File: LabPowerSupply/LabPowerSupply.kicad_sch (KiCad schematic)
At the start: 2 parts

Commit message: Began mcu placement
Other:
- sheet Primary Controller ports: added ADC 4; removed ADC 0
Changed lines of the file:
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@@
       (effects (font (size 1.27 1.27)) (justify right))
     )
-    (pin "ADC 0" input (at 182.88 71.12 180)
-      (effects (font (size 1.27 1.27)) (justify left))
-    )
-    (pin "ADC 2" input (at 182.88 76.2 180)
-      (effects (font (size 1.27 1.27)) (justify left))
-    )
-    (pin "ADC 1" input (at 182.88 73.66 180)
-      (effects (font (size 1.27 1.27)) (justify left))
-    )
-    (pin "ADC 3" input (at 182.88 78.74 180)
+    (pin "ADC 1" input (at 182.88 71.12 180)
+      (effects (font (size 1.27 1.27)) (justify left))
+    )
+    (pin "ADC 3" input (at 182.88 76.2 180)
+      (effects (font (size 1.27 1.27)) (justify left))
+    )
+    (pin "ADC 2" input (at 182.88 73.66 180)
+      (effects (font (size 1.27 1.27)) (justify left))
+    )
+    (pin "ADC 4" input (at 182.88 78.74 180)
       (effects (font (size 1.27 1.27)) (justify left))
     )
@@
       (reference "C10_Power1") (unit 1) (value "100n") (footprint "Capacitor_SMD:C_0603_1608Metric")
     )
+    (path "/0c3af00c-caea-46d1-9953-712c4efb6180/877b38b4-9fca-4c7e-a1c5-d7e6e745bcaf/f3b7bb4f-3c1d-4dfa-8749-a3a16444aa2b"
+      (reference "C_CUR1") (unit 1) (value "100n") (footprint "Capacitor_SMD:C_0603_1608Metric")
+    )
+    (path "/e157f35d-29d6-4a10-895b-6361f5380fc1/877b38b4-9fca-4c7e-a1c5-d7e6e745bcaf/f3b7bb4f-3c1d-4dfa-8749-a3a16444aa2b"
+      (reference "C_CUR2") (unit 1) (value "100n") (footprint "Capacitor_SMD:C_0603_1608Metric")
+    )
+    (path "/0c3af00c-caea-46d1-9953-712c4efb6180/1f8c5f30-7c48-4f7f-ae89-842563537cb2/8593098b-f15d-439b-8094-0023f0ebc382"
+      (reference "C_INV1") (unit 1) (value "100n") (footprint "Capacitor_SMD:C_0603_1608Metric")
+    )
+    (path "/e157f35d-29d6-4a10-895b-6361f5380fc1/1f8c5f30-7c48-4f7f-ae89-842563537cb2/8593098b-f15d-439b-8094-0023f0ebc382"
+      (reference "C_INV2") (unit 1) (value "100n") (footprint "Capacitor_SMD:C_0603_1608Metric")
+    )
+    (path "/3d294f79-f2d7-4288-8001-342bbe758cab/6678ab0e-55b4-4de2-ab64-1e272bb328a1"
+      (reference "C_OPT1") (unit 1) (value "100n") (footprint "Capacitor_SMD:C_0603_1608Metric")
+    )
+    (path "/3d294f79-f2d7-4288-8001-342bbe758cab/b5ccd18e-1d8f-4940-b38a-e2dbf67af339"
+      (reference "C_OPT2") (unit 1) (value "100n") (footprint "Capacitor_SMD:C_0603_1608Metric")
+    )
     (path "/0c3af00c-caea-46d1-9953-712c4efb6180/877b38b4-9fca-4c7e-a1c5-d7e6e745bcaf/ad5d9838-b611-434b-a2e7-188d7ef8b357"

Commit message: Started ch2 MCU routing
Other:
- sheet Primary Controller ports: added DAC 2; removed DAC 0
- sheet Secondary Controller ports: added ADC 4, DAC 2; removed ADC 0, DAC 0
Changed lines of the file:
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@@
       (effects (font (size 1.27 1.27)) (justify left top) hide)
     )
-    (pin "DAC 1" output (at 203.2 71.12 0)
+    (pin "DAC 2" output (at 203.2 71.12 0)
       (effects (font (size 1.27 1.27)) (justify right))
     )
@@
       (effects (font (size 1.27 1.27)) (justify right))
     )
-    (pin "DAC 0" output (at 203.2 68.58 0)
+    (pin "DAC 1" output (at 203.2 68.58 0)
       (effects (font (size 1.27 1.27)) (justify right))
     )
@@
       (effects (font (size 1.27 1.27)) (justify right))
     )
-    (pin "ADC 3" input (at 182.88 109.22 180)
-      (effects (font (size 1.27 1.27)) (justify left))
-    )
-    (pin "ADC 0" input (at 182.88 101.6 180)
-      (effects (font (size 1.27 1.27)) (justify left))
-    )
-    (pin "ADC 1" input (at 182.88 104.14 180)
-      (effects (font (size 1.27 1.27)) (justify left))
-    )
-    (pin "ADC 2" input (at 182.88 106.68 180)
-      (effects (font (size 1.27 1.27)) (justify left))
-    )
-    (pin "DAC 1" output (at 203.2 101.6 0)
-      (effects (font (size 1.27 1.27)) (justify right))
-    )
-    (pin "DAC 0" output (at 203.2 99.06 0)
+    (pin "ADC 4" input (at 182.88 109.22 180)
+      (effects (font (size 1.27 1.27)) (justify left))
+    )
+    (pin "ADC 1" input (at 182.88 101.6 180)
+      (effects (font (size 1.27 1.27)) (justify left))
+    )
+    (pin "ADC 2" input (at 182.88 104.14 180)
+      (effects (font (size 1.27 1.27)) (justify left))
+    )
+    (pin "ADC 3" input (at 182.88 106.68 180)
+      (effects (font (size 1.27 1.27)) (justify left))
+    )
+    (pin "DAC 2" output (at 203.2 101.6 0)
+      (effects (font (size 1.27 1.27)) (justify right))
+    )
+    (pin "DAC 1" output (at 203.2 99.06 0)
       (effects (font (size 1.27 1.27)) (justify right))
     )
@@
       (reference "J_STLink1") (unit 1) (value "Conn_01x06_Male") (footprint "Connector_PinHeader_2.54mm:PinHeader_1x06_P2.54mm_Vertical")
     )
-    (path "/67b0d6de-a54b-4bd2-af78-b383bfe8d0e6/24e68b72-506f-44a1-bcfd-b573b2c4c581"
-      (reference "J_STLink2") (unit 1) (value "Conn_01x05_Male") (footprint "Connector_PinHeader_2.54mm:PinHeader_1x05_P2.54mm_Vertical")
+    (path "/67b0d6de-a54b-4bd2-af78-b383bfe8d0e6/08b4800b-af53-4276-a503-6ae9edd2289e"
+      (reference "J_STLink2") (unit 1) (value "Conn_01x06_Male") (footprint "Connector_PinHeader_2.54mm:PinHeader_1x06_P2.54mm_Vertical")
     )
     (path "/08fd45d5-b4ab-46e8-a348-5c4ac8e52155/d2de2ac8-3643-4f24-819b-2a4facabaee8"

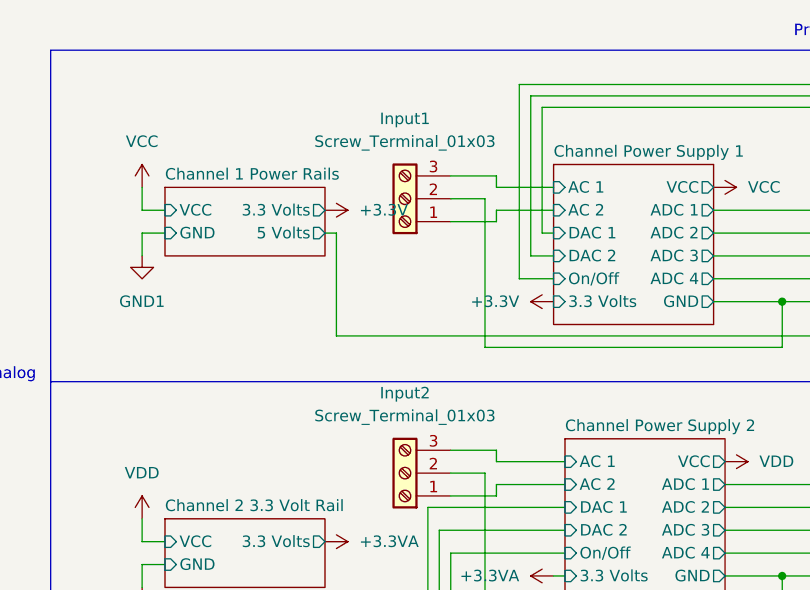
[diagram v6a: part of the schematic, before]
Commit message: Updated Part List
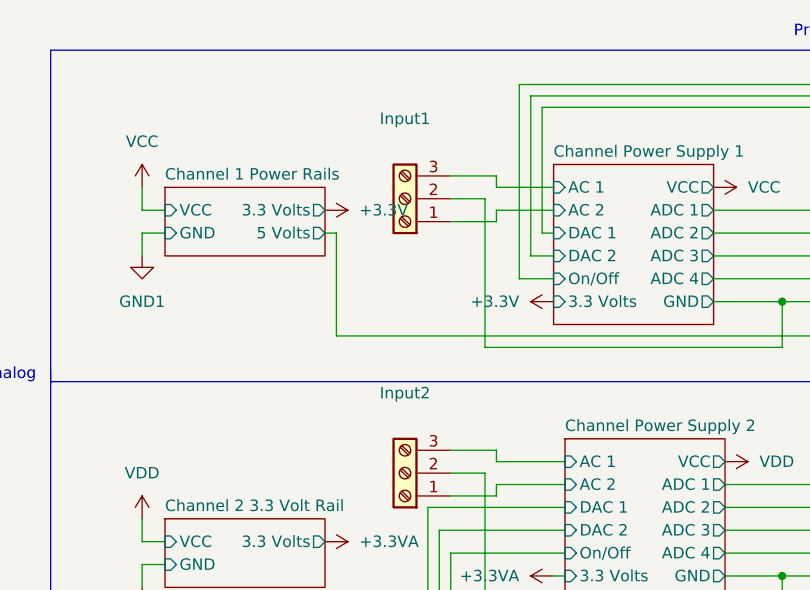
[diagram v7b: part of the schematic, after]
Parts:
- Input1, Input2: value Screw_Terminal_01x03 -> (none); footprint TerminalBlock:TerminalBlock_Altech_AK300-3_P5.00mm -> (none)
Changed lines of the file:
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@@
     (in_bom yes) (on_board yes) (fields_autoplaced)
     (property "Reference" "Input2" (id 0) (at 110.49 91.44 0))
-    (property "Value" "Screw_Terminal_01x03" (id 1) (at 110.49 93.98 0))
-    (property "Footprint" "TerminalBlock:TerminalBlock_Altech_AK300-3_P5.00mm" (id 2) (at 110.49 100.33 0)
+    (property "Value" "" (id 1) (at 110.49 93.98 0))
+    (property "Footprint" "" (id 2) (at 110.49 100.33 0)
       (effects (font (size 1.27 1.27)) hide)
     )
@@
     (in_bom yes) (on_board yes) (fields_autoplaced)
     (property "Reference" "Input1" (id 0) (at 110.49 60.96 0))
-    (property "Value" "Screw_Terminal_01x03" (id 1) (at 110.49 63.5 0))
-    (property "Footprint" "TerminalBlock:TerminalBlock_Altech_AK300-3_P5.00mm" (id 2) (at 110.49 69.85 0)
+    (property "Value" "" (id 1) (at 110.49 63.5 0))
+    (property "Footprint" "" (id 2) (at 110.49 69.85 0)
       (effects (font (size 1.27 1.27)) hide)
     )
@@
     )
     (path "/08fd45d5-b4ab-46e8-a348-5c4ac8e52155/90ba863e-1272-4db2-9d6c-45423f9bc63d"
-      (reference "A1_1") (unit 1) (value "Conn_01x01_Male") (footprint "Connector_PinHeader_2.54mm:PinHeader_1x01_P2.54mm_Vertical")
+      (reference "A1_1") (unit 1) (value "Conn_01x01_Male") (footprint "")
     )
     (path "/67b0d6de-a54b-4bd2-af78-b383bfe8d0e6/a2db6478-1e29-49c2-b0b1-c84fdb101372"
-      (reference "A1_2") (unit 1) (value "Conn_01x01_Male") (footprint "Connector_PinHeader_2.54mm:PinHeader_1x01_P2.54mm_Vertical")
+      (reference "A1_2") (unit 1) (value "Conn_01x01_Male") (footprint "")
     )
     (path "/08fd45d5-b4ab-46e8-a348-5c4ac8e52155/7b6683ab-2449-4e07-ad92-67368f0a49dc"
@@
     )
     (path "/0c3af00c-caea-46d1-9953-712c4efb6180/4d9e571f-dae1-4ed5-9f8d-0fc03fa434f7/ee1cba11-2f2c-467a-937f-a2013d595fda"
-      (reference "C5_SVR1") (unit 1) (value "1u") (footprint "Capacitor_SMD:C_0603_1608Metric")
+      (reference "C5_SVR1") (unit 1) (value "1u") (footprint "")
     )
     (path "/e157f35d-29d6-4a10-895b-6361f5380fc1/4d9e571f-dae1-4ed5-9f8d-0fc03fa434f7/ee1cba11-2f2c-467a-937f-a2013d595fda"
-      (reference "C5_SVR2") (unit 1) (value "1u") (footprint "Capacitor_SMD:C_0603_1608Metric")
+      (reference "C5_SVR2") (unit 1) (value "1u") (footprint "")
     )
     (path "/08fd45d5-b4ab-46e8-a348-5c4ac8e52155/bd5a79c6-aa46-4103-8d4f-d3095a27715e"
@@
     )
     (path "/08fd45d5-b4ab-46e8-a348-5c4ac8e52155/52649bd6-018c-4ead-b592-236b959d97d6"
-      (reference "D1_1") (unit 1) (value "Conn_01x01_Male") (footprint "Connector_PinHeader_2.54mm:PinHeader_1x01_P2.54mm_Vertical")
+      (reference "D1_1") (unit 1) (value "Conn_01x01_Male") (footprint "")
     )
     (path "/67b0d6de-a54b-4bd2-af78-b383bfe8d0e6/fc195d54-cfe4-49ac-8a71-9dd4a0dc19de"
-      (reference "D1_2") (unit 1) (value "Conn_01x01_Male") (footprint "Connector_PinHeader_2.54mm:PinHeader_1x01_P2.54mm_Vertical")
+      (reference "D1_2") (unit 1) (value "Conn_01x01_Male") (footprint "")
     )
     (path "/0c3af00c-caea-46d1-9953-712c4efb6180/ec5f87ba-0df6-4f82-8dbe-a19fd5b0d25e/9d97da99-0b25-4b48-9a49-e97a94fbcf7e"
@@
     )
     (path "/08fd45d5-b4ab-46e8-a348-5c4ac8e52155/ae4166d0-3501-472b-a768-e7fba8d8da90"
-      (reference "D2_1") (unit 1) (value "Conn_01x01_Male") (footprint "Connector_PinHeader_2.54mm:PinHeader_1x01_P2.54mm_Vertical")
+      (reference "D2_1") (unit 1) (value "Conn_01x01_Male") (footprint "")
     )
     (path "/67b0d6de-a54b-4bd2-af78-b383bfe8d0e6/87d6c3a1-7129-4354-ae7a-06b226e92bed"
-      (reference "D2_2") (unit 1) (value "Conn_01x01_Male") (footprint "Connector_PinHeader_2.54mm:PinHeader_1x01_P2.54mm_Vertical")
+      (reference "D2_2") (unit 1) (value "Conn_01x01_Male") (footprint "")
     )
     (path "/0c3af00c-caea-46d1-9953-712c4efb6180/ec5f87ba-0df6-4f82-8dbe-a19fd5b0d25e/47e36874-a349-4d76-adfa-1aaacc774a73"
@@
     )
     (path "/67b0d6de-a54b-4bd2-af78-b383bfe8d0e6/2401bd75-1fd8-478a-9cea-2d9e787b3e18"
-      (reference "J_Boot2") (unit 1) (value "Conn_01x03_Male") (footprint "Connector_PinHeader_2.54mm:PinHeader_1x03_P2.54mm_Vertical")
+      (reference "J_Boot2") (unit 1) (value "Conn_01x03_Male") (footprint "")
     )
     (path "/08fd45d5-b4ab-46e8-a348-5c4ac8e52155/4562e315-4764-4c90-b39e-6cfb51f79e8b"
